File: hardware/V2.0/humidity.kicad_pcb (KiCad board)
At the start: 2 copper layers, 15 x 25 mm, 21 parts, among them P101 CON-SENSOR2, P102 BOOT, U101 XMC1XXX24, U102 SHT3x-DIS, U103 DRILL, U104 DRILL, U105 DRILL, U106 DRILL

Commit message: fiducials added
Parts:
- added Fiducial_Mark: VAL**, kicad-libraries:Fiducial_Mark, F.Cu at (147.6, 152.0)
- added Fiducial_Mark: VAL**, kicad-libraries:Fiducial_Mark, F.Cu at (153.6, 137.5)
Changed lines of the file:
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@@
     (tracks 171)
     (zones 0)
-    (modules 21)
+    (modules 23)
     (nets 17)
   )
   (page A4)
   (layers
-    (0 F.Cu signal hide)
+    (0 F.Cu signal)
     (31 B.Cu signal hide)
     (32 B.Adhes user)
@@
   )
   (setup
-    (last_trace_width 0.25)
+    (last_trace_width 0.2)
     (user_trace_width 0.25)
     (user_trace_width 0.3)
@@
       (xy 2.3114 -1.41732) (xy 2.3114 -1.67132) (xy 2.3114 -1.67132)) (layer B.SilkS) (width 0.00254))
   )
+  (module kicad-libraries:Fiducial_Mark (layer F.Cu)
+    (at 147.6 152)
+    (attr smd)
+    (fp_text reference Fiducial_Mark (at 0 0) (layer F.SilkS) hide
+      (effects (font (size 0.127 0.127) (thickness 0.03302)))
+    )
+    (fp_text value VAL** (at 0 -0.29972) (layer F.SilkS) hide
+      (effects (font (size 0.127 0.127) (thickness 0.03302)))
+    )
+    (fp_circle (center 0 0) (end 1.15062 0) (layer Dwgs.User) (width 0.01016))
+    (pad 1 smd circle (at 0 0) (size 1.00076 1.00076) (layers F.Cu F.Paste F.Mask)
+      (clearance 0.65024))
+  )
+  (module kicad-libraries:Fiducial_Mark (layer F.Cu)
+    (at 153.6 137.5)
+    (attr smd)
+    (fp_text reference Fiducial_Mark (at 0 0) (layer F.SilkS) hide
+      (effects (font (size 0.127 0.127) (thickness 0.03302)))
+    )
+    (fp_text value VAL** (at 0 -0.29972) (layer F.SilkS) hide
+      (effects (font (size 0.127 0.127) (thickness 0.03302)))
+    )
+    (fp_circle (center 0 0) (end 1.15062 0) (layer Dwgs.User) (width 0.01016))
+    (pad 1 smd circle (at 0 0) (size 1.00076 1.00076) (layers F.Cu F.Paste F.Mask)
+      (clearance 0.65024))
+  )
   (gr_text 2.0 (at 150.1 134.9 90) (layer F.SilkS)

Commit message: fix i2c routing
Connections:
- U101 pad 17: SCL -> SDA
- U101 pad 19: SDA -> SCL
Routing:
- net SCL: track 5.97 -> 8.29 mm, vias 0 -> 2
- net SDA: track 5.57 -> 6.60 mm
- net VCC: track 38.2 -> 37.6 mm
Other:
- board text added: "Humidity"
- board text removed: "humidity"
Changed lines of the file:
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@@
     (thickness 1.6)
     (drawings 12)
-    (tracks 171)
+    (tracks 184)
     (zones 0)
     (modules 23)
@@
   (layers
     (0 F.Cu signal)
-    (31 B.Cu signal hide)
+    (31 B.Cu signal)
     (32 B.Adhes user)
     (33 F.Adhes user)
@@
   )
   (setup
-    (last_trace_width 0.2)
+    (last_trace_width 0.25)
     (user_trace_width 0.25)
     (user_trace_width 0.3)
@@
     (pad 16 smd oval (at 2.025 -0.25 225) (size 1 0.3) (layers F.Cu F.Paste F.Mask))
     (pad 17 smd oval (at 2.025 -0.75 225) (size 1 0.3) (layers F.Cu F.Paste F.Mask)
-      (net 12 SCL))
+      (net 10 SDA))
     (pad 18 smd oval (at 2.025 -1.25 225) (size 1 0.3) (layers F.Cu F.Paste F.Mask))
     (pad 19 smd oval (at 1.25 -2.025 315) (size 1 0.3) (layers F.Cu F.Paste F.Mask)
-      (net 10 SDA))
+      (net 12 SCL))
     (pad 20 smd oval (at 0.75 -2.025 315) (size 1 0.3) (layers F.Cu F.Paste F.Mask))
     (pad 21 smd oval (at 0.25 -2.025 315) (size 1 0.3) (layers F.Cu F.Paste F.Mask)
@@
     (effects (font (size 0.7 0.7) (thickness 0.15)))
   )
-  (gr_text humidity (at 147.3 135.6 90) (layer F.SilkS)
+  (gr_text Humidity (at 147.4 135.6 90) (layer F.SilkS)
     (effects (font (size 0.7 0.7) (thickness 0.15)))
   )
@@
   (segment (start 142.4 135.846447) (end 142.4 135.13934) (width 0.25) (layer F.Cu) (net 1))
   (segment (start 142.4 135.13934) (end 142.23033 134.96967) (width 0.25) (layer F.Cu) (net 1))
+  (segment (start 142 141.1) (end 142 140.7) (width 0.25) (layer F.Cu) (net 2))
+  (segment (start 140.8 139.5) (end 140.8 136.4) (width 0.25) (layer F.Cu) (net 2))
+  (segment (start 142 140.7) (end 140.8 139.5) (width 0.25) (layer F.Cu) (net 2))
+  (segment (start 140.8 146.5) (end 140.8 144.2) (width 0.25) (layer F.Cu) (net 2))
+  (segment (start 142 141.1) (end 143.1 141.1) (width 0.25) (layer B.Cu) (net 2))
+  (via (at 142 141.1) (size 0.55) (drill 0.25) (layers F.Cu B.Cu) (net 2))
+  (segment (start 142 143) (end 142 141.1) (width 0.25) (layer F.Cu) (net 2))
+  (segment (start 140.8 144.2) (end 142 143) (width 0.25) (layer F.Cu) (net 2))
   (segment (start 147 142.45) (end 146.65 142.45) (width 0.25) (layer F.Cu) (net 2))
   (segment (start 146.65 142.45) (end 146.05 141.85) (width 0.25) (layer F.Cu) (net 2))
@@
   (segment (start 140.75 135.61066) (end 141.16967 136.03033) (width 0.25) (layer F.Cu) (net 2))
   (segment (start 141.16967 136.03033) (end 140.8 136.4) (width 0.25) (layer F.Cu) (net 2))
-  (segment (start 140.8 141.9) (end 141.3 142.4) (width 0.25) (layer F.Cu) (net 2))
-  (segment (start 140.8 136.4) (end 140.8 141.9) (width 0.25) (layer F.Cu) (net 2))
   (segment (start 148.5 142.39924) (end 147.05076 142.39924) (width 0.5) (layer F.Cu) (net 2))
   (segment (start 147.05076 142.39924) (end 147 142.45) (width 0.5) (layer F.Cu) (net 2))
@@
   (segment (start 141.9 146.75) (end 141.05 146.75) (width 0.25) (layer F.Cu) (net 2))
   (segment (start 141.05 146.75) (end 140.8 146.5) (width 0.25) (layer F.Cu) (net 2))
-  (segment (start 140.8 146.5) (end 140.8 142.9) (width 0.25) (layer F.Cu) (net 2))
-  (segment (start 140.8 142.9) (end 141.3 142.4) (width 0.25) (layer F.Cu) (net 2))
   (segment (start 143.1 141.1) (end 143.3 141.1) (width 0.25) (layer F.Cu) (net 2))
-  (via (at 141.3 142.4) (size 0.55) (drill 0.25) (layers F.Cu B.Cu) (net 2))
-  (segment (start 141.3 142.4) (end 142.6 141.1) (width 0.25) (layer B.Cu) (net 2))
-  (segment (start 142.6 141.1) (end 143.1 141.1) (width 0.25) (layer B.Cu) (net 2))
   (via (at 143.1 141.1) (size 0.55) (drill 0.25) (layers F.Cu B.Cu) (net 2))
   (segment (start 143.35 147.225) (end 142.875 146.75) (width 0.25) (layer F.Cu) (net 2))
@@
   (segment (start 143.6 134.4) (end 144.85 134.4) (width 0.25) (layer F.Cu) (net 9))
   (segment (start 144.85 134.4) (end 145.41967 133.83033) (width 0.25) (layer F.Cu) (net 9))
-  (segment (start 144.648008 140.215775) (end 145.332233 140.9) (width 0.25) (layer F.Cu) (net 10))
-  (segment (start 145.5 141.8) (end 144.5 142.8) (width 0.25) (layer B.Cu) (net 10))
-  (segment (start 145.5 140.9) (end 145.5 141.8) (width 0.25) (layer B.Cu) (net 10))
-  (via (at 145.5 140.9) (size 0.55) (drill 0.25) (layers F.Cu B.Cu) (net 10))
-  (segment (start 145.332233 140.9) (end 145.5 140.9) (width 0.25) (layer F.Cu) (net 10))
-  (segment (start 144.5 142.8) (end 144.5 143.54968) (width 0.25) (layer F.Cu) (net 10))
+  (segment (start 144.49878 143.5509) (end 144.49878 142.80122) (width 0.2) (layer F.Cu) (net 10))
+  (segment (start 142.66066 140.4) (end 143.198439 139.862221) (width 0.2) (layer F.Cu) (net 10))
+  (segment (start 142.6 140.4) (end 142.66066 140.4) (width 0.2) (layer F.Cu) (net 10))
+  (via (at 142.6 140.4) (size 0.55) (drill 0.25) (layers F.Cu B.Cu) (net 10))
+  (segment (start 143.4 140.4) (end 142.6 140.4) (width 0.2) (layer B.Cu) (net 10))
+  (segment (start 144 141) (end 143.4 140.4) (width 0.2) (layer B.Cu) (net 10))
+  (segment (start 144 142.3) (end 144 141) (width 0.2) (layer B.Cu) (net 10))
+  (segment (start 144.5 142.8) (end 144 142.3) (width 0.2) (layer B.Cu) (net 10))
   (via (at 144.5 142.8) (size 0.55) (drill 0.25) (layers F.Cu B.Cu) (net 10))
+  (segment (start 144.49878 142.80122) (end 144.5 142.8) (width 0.2) (layer F.Cu) (net 10))
   (segment (start 144.5 143.54968) (end 144.49878 143.5509) (width 0.25) (layer F.Cu) (net 10))
   (segment (start 144.85 144.775) (end 144.85 144.35) (width 0.25) (layer F.Cu) (net 10))
@@
   (segment (start 144.3 148.6) (end 145 148.6) (width 0.25) (layer F.Cu) (net 11))
   (segment (start 143.85 148.15) (end 144.3 148.6) (width 0.25) (layer F.Cu) (net 11))
-  (segment (start 143.198439 139.862221) (end 142 141.06066) (width 0.25) (layer F.Cu) (net 12))
-  (segment (start 142 142.64978) (end 142.90112 143.5509) (width 0.25) (layer F.Cu) (net 12))
-  (segment (start 142 141.06066) (end 142 142.64978) (width 0.25) (layer F.Cu) (net 12))
+  (segment (start 145.5 140.9) (end 145.5 142.2) (width 0.2) (layer B.Cu) (net 12))
+  (segment (start 143.5 143.4) (end 142.9 142.8) (width 0.2) (layer B.Cu) (net 12))
+  (segment (start 144.9 143.4) (end 143.5 143.4) (width 0.2) (layer B.Cu) (net 12))
+  (segment (start 145.2 143.1) (end 144.9 143.4) (width 0.2) (layer B.Cu) (net 12))
+  (segment (start 145.2 142.5) (end 145.2 143.1) (width 0.2) (layer B.Cu) (net 12))
+  (segment (start 145.5 142.2) (end 145.2 142.5) (width 0.2) (layer B.Cu) (net 12))
+  (segment (start 144.648008 140.215775) (end 145.332233 140.9) (width 0.2) (layer F.Cu) (net 12))
+  (segment (start 142.9 142.8) (end 142.9 143.54978) (width 0.2) (layer F.Cu) (net 12))
+  (via (at 142.9 142.8) (size 0.55) (drill 0.25) (layers F.Cu B.Cu) (net 12))
+  (via (at 145.5 140.9) (size 0.55) (drill 0.25) (layers F.Cu B.Cu) (net 12))
+  (segment (start 145.332233 140.9) (end 145.5 140.9) (width 0.2) (layer F.Cu) (net 12))
+  (segment (start 142.9 143.54978) (end 142.90112 143.5509) (width 0.2) (layer F.Cu) (net 12))
   (segment (start 143.35 144.775) (end 143.35 144.35) (width 0.25) (layer F.Cu) (net 12))
   (segment (start 143.35 144.35) (end 142.90112 143.90112) (width 0.25) (layer F.Cu) (net 12))

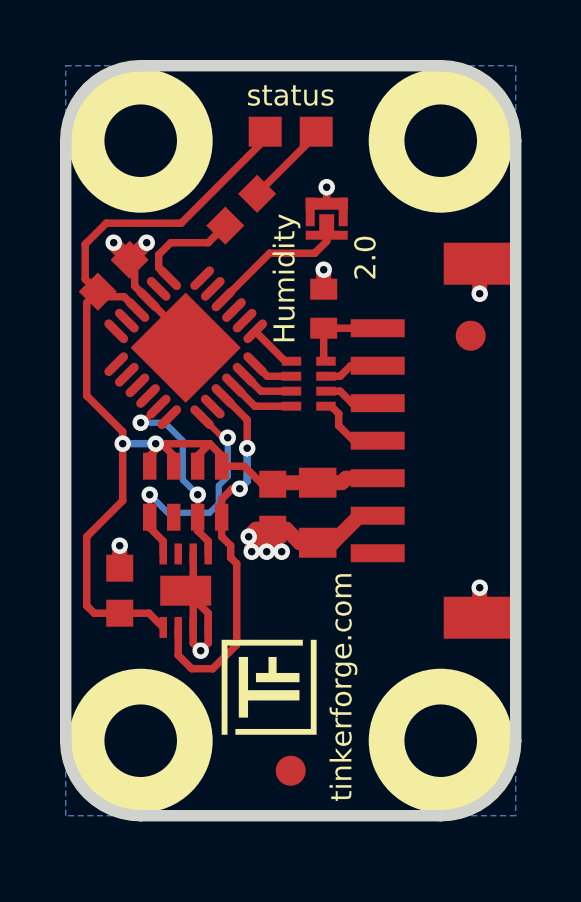
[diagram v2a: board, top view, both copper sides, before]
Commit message: add debug pad
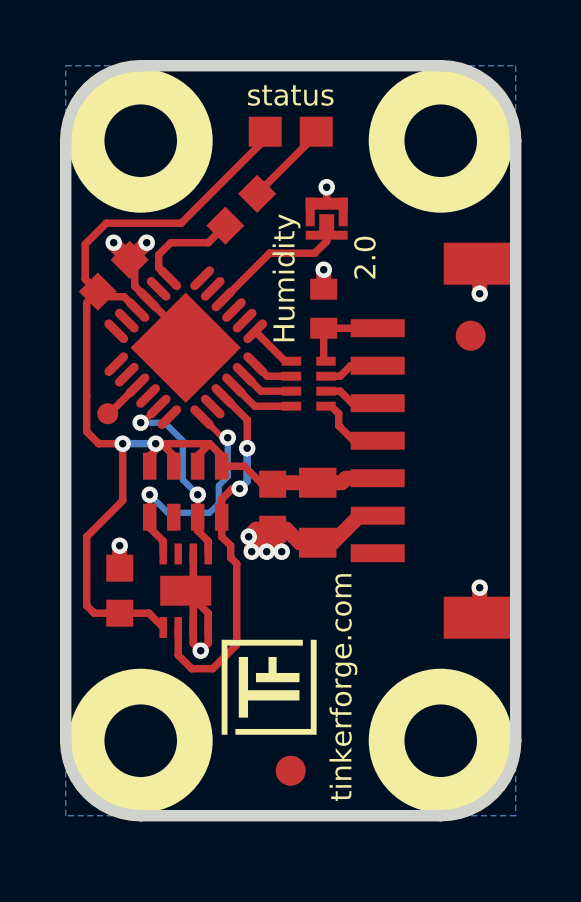
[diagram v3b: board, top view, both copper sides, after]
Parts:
- added P103: DEBUG, kicad-libraries:DEBUG_PAD, F.Cu at (141.5, 140.1)
- turned VAL to 270 degrees
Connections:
- U101 pad 15: (no net) -> Net-(P103-Pad1)
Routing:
- net Net-(P103-Pad1): track 0.00 -> 1.38 mm
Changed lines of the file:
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@@
 (kicad_pcb (version 4) (host pcbnew 4.0.2+e4-6225~38~ubuntu15.10.1-stable)
   (general
-    (links 49)
+    (links 50)
     (no_connects 0)
     (area 139.909499 128.309499 155.290501 153.690501)
     (thickness 1.6)
     (drawings 12)
-    (tracks 184)
+    (tracks 187)
     (zones 0)
-    (modules 23)
-    (nets 17)
+    (modules 24)
+    (nets 18)
   )
   (page A4)
@@
     (trace_clearance 0.15)
     (zone_clearance 0.2)
-    (zone_45_only no)
+    (zone_45_only yes)
     (trace_min 0.15)
     (segment_width 0.381)
@@
     (pad_to_mask_clearance 0)
     (aux_axis_origin 0 0)
-    (visible_elements FFFF7F7F)
+    (visible_elements FFFF7F5F)
     (pcbplotparams
       (layerselection 0x00030_80000001)
@@
   (net 15 S-CLK)
   (net 16 S-MOSI)
+  (net 17 "Net-(P103-Pad1)")
   (net_class Default "This is the default net class."
     (clearance 0.15)
@@
     (add_net "Net-(P101-Pad6)")
     (add_net "Net-(P102-Pad2)")
+    (add_net "Net-(P103-Pad1)")
     (add_net "Net-(R101-Pad1)")
     (add_net S-CLK)
@@
     (pad 13 smd oval (at 2.025 1.25 225) (size 1 0.3) (layers F.Cu F.Paste F.Mask))
     (pad 14 smd oval (at 2.025 0.75 225) (size 1 0.3) (layers F.Cu F.Paste F.Mask))
-    (pad 15 smd oval (at 2.025 0.25 225) (size 1 0.3) (layers F.Cu F.Paste F.Mask))
+    (pad 15 smd oval (at 2.025 0.25 225) (size 1 0.3) (layers F.Cu F.Paste F.Mask)
+      (net 17 "Net-(P103-Pad1)"))
     (pad 16 smd oval (at 2.025 -0.25 225) (size 1 0.3) (layers F.Cu F.Paste F.Mask))
     (pad 17 smd oval (at 2.025 -0.75 225) (size 1 0.3) (layers F.Cu F.Paste F.Mask)
@@
   )
   (module kicad-libraries:CE_5mm (layer B.Cu)
-    (at 147.6 146.7 90)
-    (fp_text reference VAL (at 0 0 90) (layer B.SilkS) hide
+    (at 147.6 146.7 270)
+    (fp_text reference VAL (at 0 0 270) (layer B.SilkS) hide
       (effects (font (size 1.143 1.143) (thickness 0.1778)) (justify mirror))
     )
-    (fp_text value CE_5mm (at 0 0 90) (layer B.SilkS) hide
+    (fp_text value CE_5mm (at 0 0 270) (layer B.SilkS) hide
       (effects (font (size 1.143 1.143) (thickness 0.1778)) (justify mirror))
     )
@@
       (clearance 0.65024))
   )
+  (module kicad-libraries:DEBUG_PAD (layer F.Cu)
+    (at 141.5 140.1)
+    (fp_text reference P103 (at 0 0.175) (layer F.Fab)
+      (effects (font (size 0.15 0.15) (thickness 0.0375)))
+    )
+    (fp_text value DEBUG (at 0 -0.15) (layer F.Fab)
+      (effects (font (size 0.15 0.15) (thickness 0.0375)))
+    )
+    (pad 1 smd circle (at 0 0) (size 0.7 0.7) (layers F.Cu F.Paste F.Mask)
+      (net 17 "Net-(P103-Pad1)"))
+  )
   (gr_text 2.0 (at 150.1 134.9 90) (layer F.SilkS)
     (effects (font (size 0.7 0.7) (thickness 0.15)))
@@
   (segment (start 142.4 135.846447) (end 142.4 135.13934) (width 0.25) (layer F.Cu) (net 1))
   (segment (start 142.4 135.13934) (end 142.23033 134.96967) (width 0.25) (layer F.Cu) (net 1))
-  (segment (start 142 141.1) (end 142 140.7) (width 0.25) (layer F.Cu) (net 2))
+  (segment (start 142 141.1) (end 141.2 141.1) (width 0.25) (layer F.Cu) (net 2))
+  (segment (start 140.8 140.7) (end 140.8 139.5) (width 0.25) (layer F.Cu) (net 2))
+  (segment (start 141.2 141.1) (end 140.8 140.7) (width 0.25) (layer F.Cu) (net 2))
   (segment (start 140.8 139.5) (end 140.8 136.4) (width 0.25) (layer F.Cu) (net 2))
-  (segment (start 142 140.7) (end 140.8 139.5) (width 0.25) (layer F.Cu) (net 2))
+  (segment (start 141.16967 136.03033) (end 140.8 136.4) (width 0.25) (layer F.Cu) (net 2))
   (segment (start 140.8 146.5) (end 140.8 144.2) (width 0.25) (layer F.Cu) (net 2))
   (segment (start 142 141.1) (end 143.1 141.1) (width 0.25) (layer B.Cu) (net 2))
@@
   (segment (start 140.75 134.45) (end 140.75 135.61066) (width 0.25) (layer F.Cu) (net 2))
   (segment (start 140.75 135.61066) (end 141.16967 136.03033) (width 0.25) (layer F.Cu) (net 2))
-  (segment (start 141.16967 136.03033) (end 140.8 136.4) (width 0.25) (layer F.Cu) (net 2))
   (segment (start 148.5 142.39924) (end 147.05076 142.39924) (width 0.5) (layer F.Cu) (net 2))
   (segment (start 147.05076 142.39924) (end 147 142.45) (width 0.5) (layer F.Cu) (net 2))
@@
   (segment (start 146.415775 138.448008) (end 146.818847 138.85108) (width 0.25) (layer F.Cu) (net 16))
   (segment (start 146.818847 138.85108) (end 147.625 138.85108) (width 0.25) (layer F.Cu) (net 16))
+  (segment (start 142.491332 139.155115) (end 141.546447 140.1) (width 0.25) (layer F.Cu) (net 17))
+  (segment (start 141.546447 140.1) (end 141.5 140.1) (width 0.25) (layer F.Cu) (net 17))
   (zone (net 1) (net_name GND) (layer B.Cu) (hatch edge 0.508)
     (connect_pads yes (clearance 0.2))
@@
       )
     )
+  )
+  (zone (net 0) (net_name "") (layer B.Cu) (hatch edge 0.508)
+    (connect_pads (clearance 0.2))
+    (min_thickness 0.2)
+    (keepout (tracks allowed) (vias allowed) (copperpour not_allowed))
+    (fill (arc_segments 16) (thermal_gap 0.21) (thermal_bridge_width 0.21))
+    (polygon
+      (pts
+        (xy 140.1 144.1) (xy 140.1 143.2) (xy 145.5 143.2) (xy 145.5 144.1) (xy 145.4 144.1)
+      )
+    )
